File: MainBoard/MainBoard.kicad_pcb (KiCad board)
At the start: 6 copper layers, 45 x 45 mm, 110 parts, among them J1 0015912060 Molex, J2 USB4110-GF-A, J3 M55-7104042R, Q1 PMV19XNEAR, Q2 PMV19XNEAR, Q3 PMV19XNEAR, Q4 PMV19XNEAR, SW1 SW_TL1015AF160QG, SW2 SW_TL1015AF160QG, U1 INA185A4IDRLR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

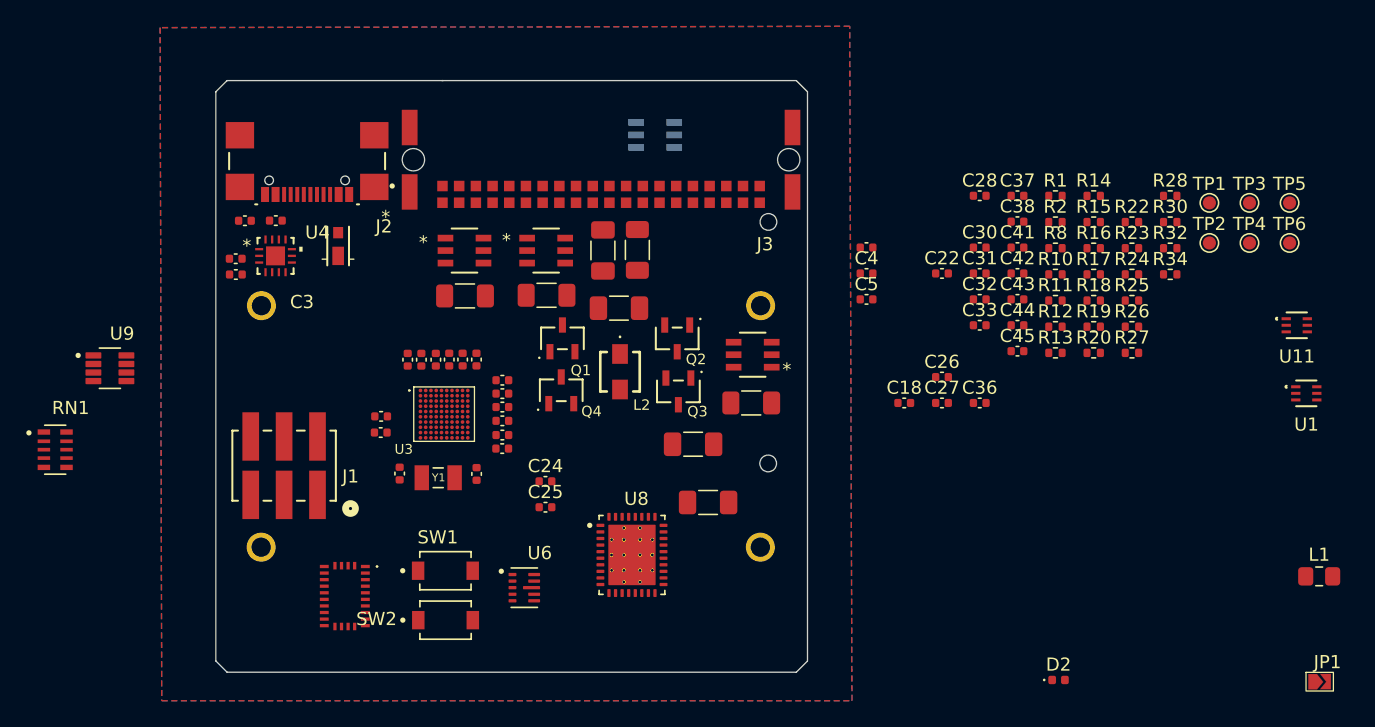
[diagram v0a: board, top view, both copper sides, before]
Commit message: Waiting on board sizes to finish placement
All parts placed, some light schematic and checking work still needs to be done
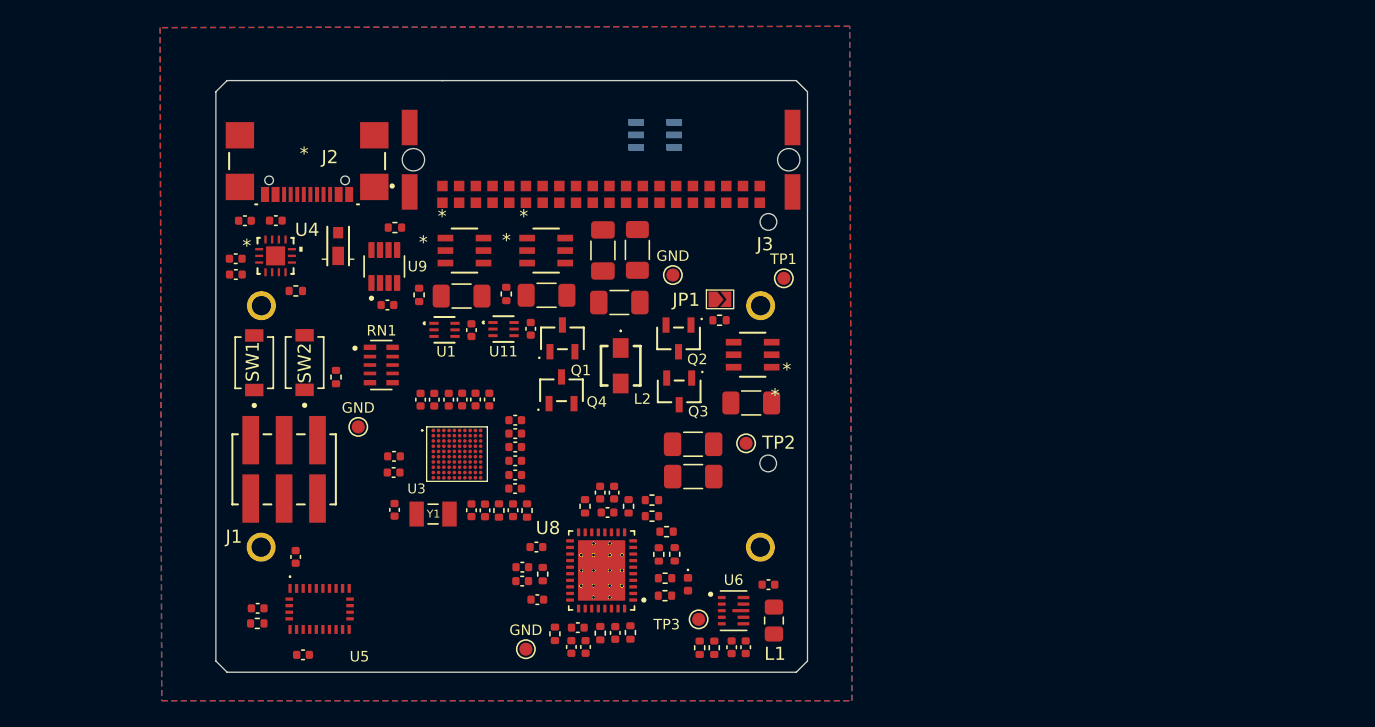
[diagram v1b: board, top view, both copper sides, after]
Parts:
- removed TP4: GND, TestPoint:TestPoint_Pad_D1.0mm
- added GND: GND, TestPoint:TestPoint_Pad_D1.0mm, F.Cu at (104.2, 56.5)
- moved GND 72.9 mm to (80.2, 68.1)
- moved R10 66.3 mm to (72.5, 83.0)
- moved GND 65.8 mm to (93.0, 85.0)
- moved U1 65.7 mm to (86.8, 60.7)
- moved R22 61.7 mm to (78.5, 64.3), turned to -90 degrees
- moved U11 60.3 mm to (91.3, 60.7)
- moved R8 57.9 mm to (75.5, 57.8)
- moved R32 57.2 mm to (84.9, 58.1), turned to 90 degrees
- moved R25 56.3 mm to (83.0, 52.9), turned to 180 degrees
- moved JP1 54.1 mm to (107.7, 58.4)
- moved C22 53.7 mm to (75.5, 78.0), turned to 90 degrees
- moved R23 52.8 mm to (95.2, 83.8), turned to -90 degrees
- moved TP3 52.5 mm to (106.1, 82.7)
- moved C5 51.9 mm to (72.6, 81.9)
- moved C4 51.8 mm to (76.0, 85.4), turned to 180 degrees
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- renumbered TP6 to GND, TP5 to GND

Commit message: Still waiting on final board size....
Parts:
- added R35: 100k, Resistor_SMD:R_0402_1005Metric, B.Cu at (108.5, 46.0)
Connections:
- U2 pad 3: unconnected-(U2-G-Pad3) -> HEATER_ENABLE
- U2 pad 4: unconnected-(U2-S-Pad4) -> BAT+
- U3 pad E1: unconnected-(U3A-PC8-PadE1) -> HEATER_ENABLE
- U3 pad E4: unconnected-(U3A-PC7-PadE4) -> EXTERNAL_BAT_CUTOFF
- U3 pad F3: unconnected-(U3A-PD14-PadF3) -> BAT_PULLDOWN
- U3 pad G4: unconnected-(U3A-PE14-PadG4) -> IMU_NRST
- U3 pad H4: unconnected-(U3A-PE15-PadH4) -> IMU_PSO/WAKE_GPIO
- U3 pad J5: unconnected-(U3A-PE9-PadJ5) -> BATMANG_INT_DIN
- U3 pad K4: unconnected-(U3A-PE11-PadK4) -> EXTERNAL_3.3V_CUTOFF
- U3 pad K5: unconnected-(U3A-PE8-PadK5) -> IMU_PSO/WAKE_GPIO
- U3 pad K6: unconnected-(U3A-PE7-PadK6) -> USBC_PD_INT_N
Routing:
- net +3.3V: track 0.00 -> 42.3 mm, vias 0 -> 7
- net USB_D-: track 0.00 -> 2.08 mm, vias 0 -> 1
- net USB_D+: track 0.00 -> 2.08 mm, vias 0 -> 1
- net GND: track 0.00 -> 1.18 mm, vias 0 -> 6
- net USBC_PD_INT_N: vias 0 -> 1
- net SWO: vias 0 -> 1
- net PARENT_SPI3_SCK: vias 0 -> 1
- net PARENT_SPI3_NSS: vias 0 -> 1
- net PARENT_SPI3_MOSI: vias 0 -> 1
- net PARENT_SPI3_MISO: vias 0 -> 1
- net Net-(U3A-PC15-OSC32_OUT): vias 0 -> 1
- net Net-(U3A-PC14-OSC32_IN): vias 0 -> 1
- net Net-(U3A-PA2): vias 0 -> 1
- net Net-(U3A-PA1): vias 0 -> 1
- net NRST: vias 0 -> 1
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
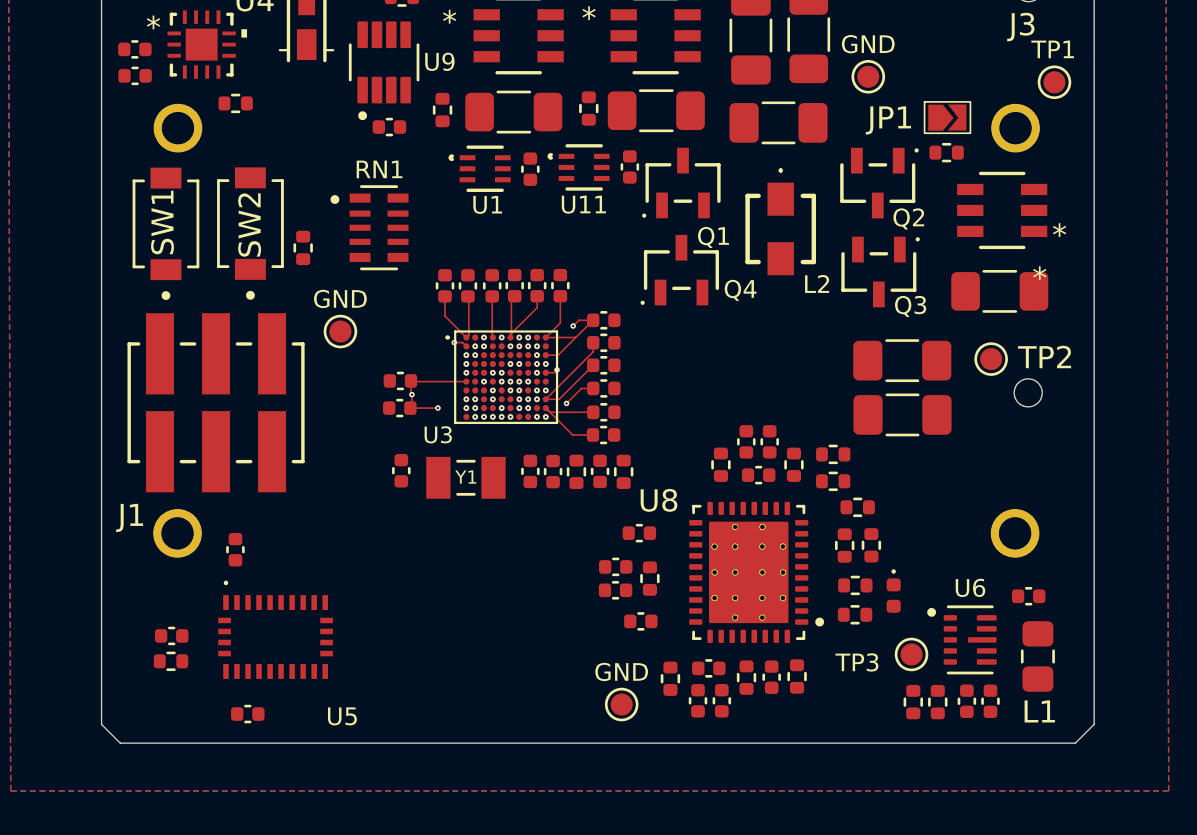
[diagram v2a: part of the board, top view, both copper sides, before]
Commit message: Cap routing
Capacitor Routing near STM, can be moved around if needed
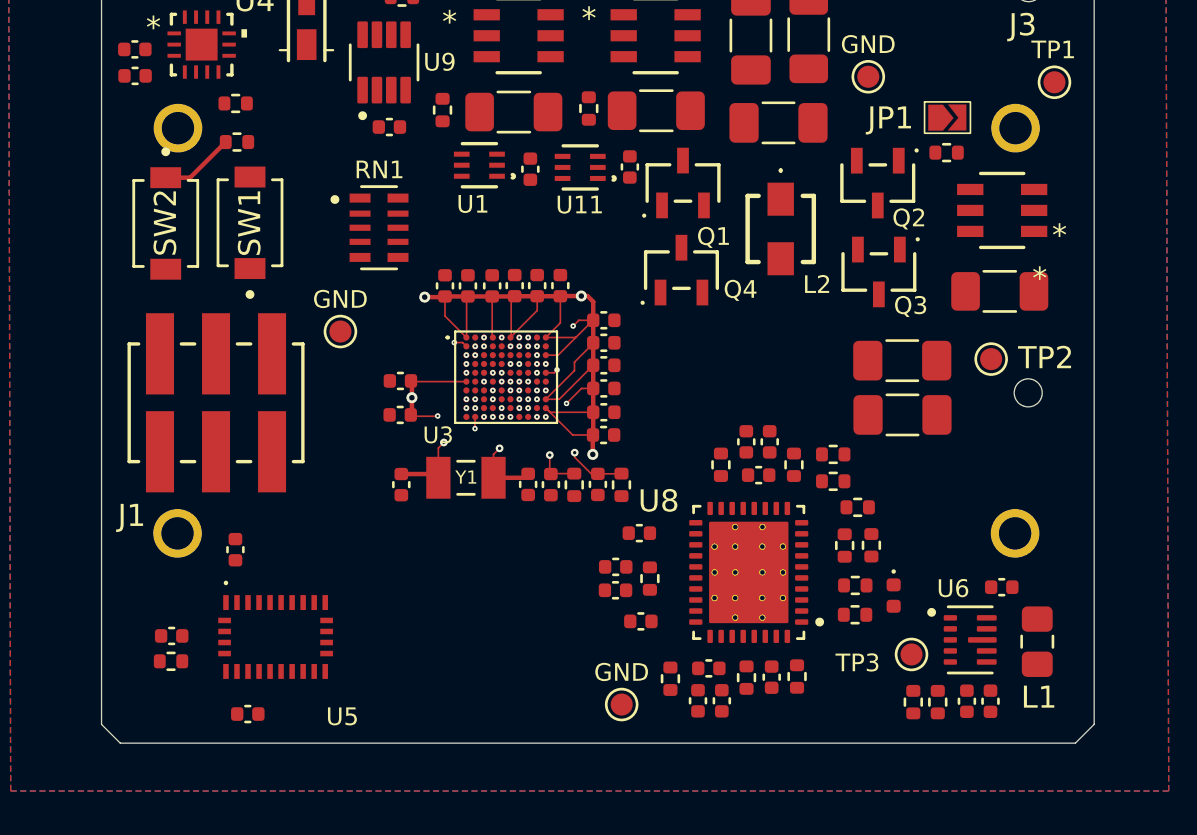
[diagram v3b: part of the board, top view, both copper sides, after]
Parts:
- moved R22 5.66 mm to (75.5, 59.5), turned to 180 degrees
- moved SW2 3.84 mm to (72.3, 63.2), turned to -90 degrees
- moved SW1 3.81 mm to (76.1, 63.2)
- moved C18 1.29 mm to (110.2, 79.7)
- moved L1 0.67 mm to (111.8, 82.2)
- moved C29 0.63 mm to (83.0, 75.0)
- moved C24 0.60 mm to (89.8, 75.0)
- moved C46 0.60 mm to (88.7, 75.0)
- moved R1 0.60 mm to (90.8, 75.0)
- moved C25 0.60 mm to (91.9, 75.0)
- moved R2 0.60 mm to (93.0, 75.0)
- moved C17 0.31 mm to (82.9, 71.9)
- moved U1 0.31 mm to (86.5, 60.6), turned to 180 degrees
- moved U11 0.18 mm to (91.1, 60.7), turned to 180 degrees
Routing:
- net +3.3V: track 42.3 -> 57.1 mm, vias 7 -> 10
- net Net-(U3A-PC15-OSC32_OUT): track 0.00 -> 10.8 mm, vias 1 -> 2
- net Net-(U3A-PC14-OSC32_IN): track 0.00 -> 8.81 mm, vias 1 -> 2
- net Net-(U3A-PA2): track 0.00 -> 6.14 mm, vias 1 -> 2
- net Net-(U3A-PA1): track 0.00 -> 5.66 mm, vias 1 -> 2
- net BOOT0: track 0.00 -> 3.39 mm
- net GND: track 1.18 -> 1.72 mm

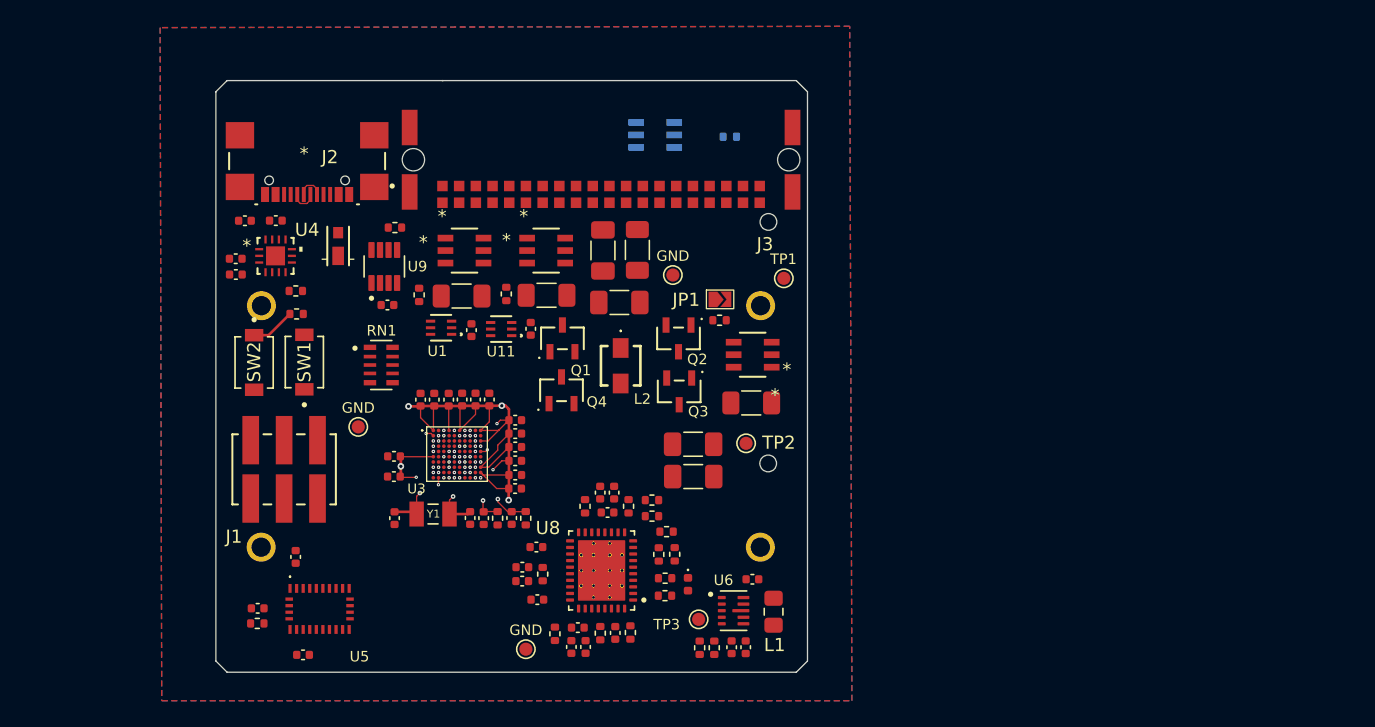
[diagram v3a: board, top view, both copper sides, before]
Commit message: Happy with placement
Got sizes from mechanical, adjusted placement accordingly
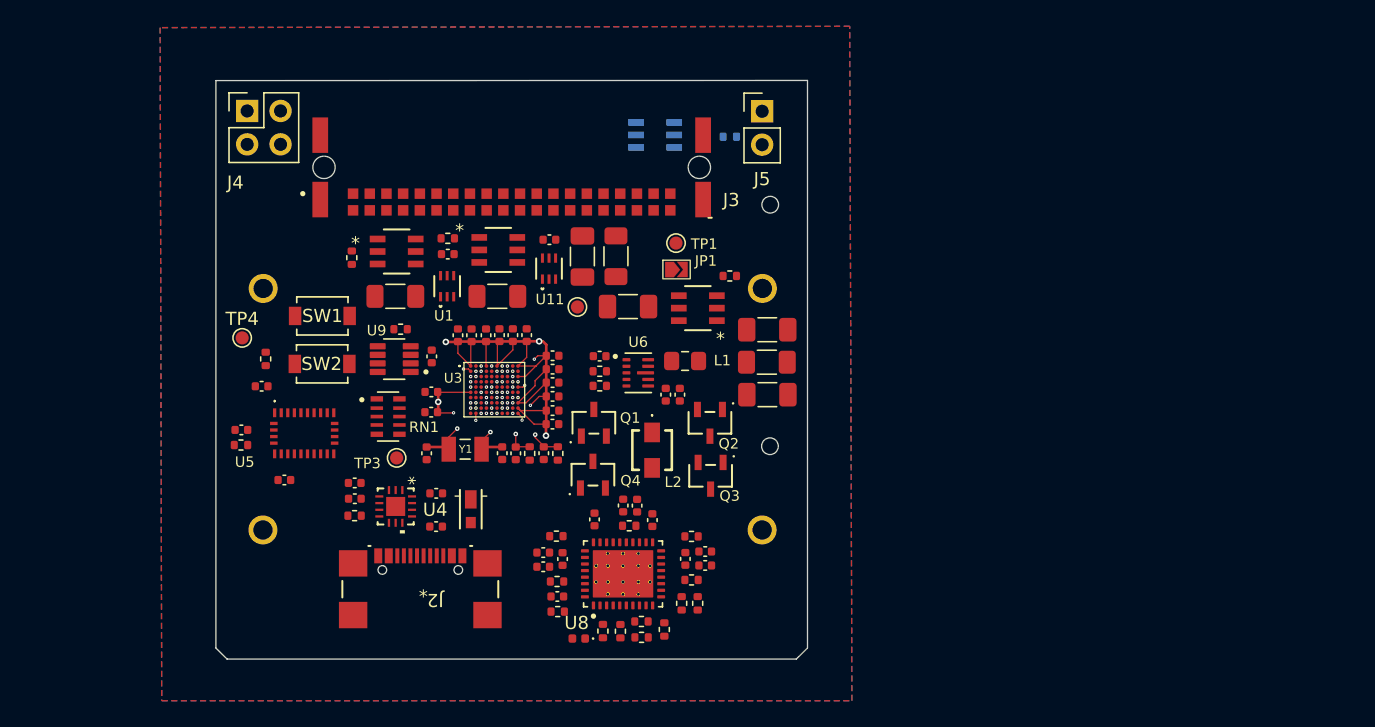
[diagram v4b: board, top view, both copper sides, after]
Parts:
- removed GND (x3): GND, TestPoint:TestPoint_Pad_D1.0mm
- removed J1: 0015912060 Molex, inspirefly:CONN_713080000-SD_06_M6p10_MOL
- added J4: Conn_01x04_Pin, Connector_PinHeader_2.54mm:PinHeader_2x02_P2.54mm_Vertical, F.Cu at (71.8, 44.1)
- added J5: Conn_01x02_Pin, Connector_PinHeader_2.54mm:PinHeader_1x02_P2.54mm_Vertical, F.Cu at (111.0, 44.1)
- added TP4: GND, TestPoint:TestPoint_Pad_D1.0mm, F.Cu at (71.4, 61.3)
- moved J2 35.3 mm to (85.0, 81.3), turned to 0 degrees
- moved C7 26.3 mm to (86.2, 75.7)
- moved TP3 26.0 mm to (83.2, 70.5)
- moved C6 25.3 mm to (86.2, 73.2), turned to 0 degrees
- moved D1 22.4 mm to (88.8, 74.4), turned to -90 degrees
- moved R12 22.4 mm to (98.6, 63.9), turned to 180 degrees
- moved R11 21.7 mm to (98.6, 65.0), turned to 180 degrees
- moved U4 21.1 mm to (83.1, 74.2), turned to -90 degrees
- moved C18 20.6 mm to (98.6, 62.7), turned to 180 degrees
- moved L1 20.2 mm to (105.1, 63.1), turned to 0 degrees
- moved C26 19.9 mm to (104.7, 65.7)
- moved C27 19.9 mm to (103.6, 65.7)
- moved BT2 19.7 mm to (92.0, 57.6)
- moved U6 19.5 mm to (101.5, 64.0)
- moved C1 19.3 mm to (80.0, 72.4)
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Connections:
- J3 pad B11: EXTERNAL_VOLTAGE -> GND
- J3 pad B12: EXTERNAL_VOLTAGE -> unconnected-(J3-PadB12)
- J3 pad B13: EXTERNAL_VOLTAGE -> unconnected-(J3-PadB13)
- J3 pad B14: EXTERNAL_VOLTAGE -> unconnected-(J3-PadB14)
- J3 pad B15: unconnected-(J3-PadB15) -> EXTERNAL_VOLTAGE
- J3 pad B16: unconnected-(J3-PadB16) -> EXTERNAL_VOLTAGE
- J3 pad B17: unconnected-(J3-PadB17) -> EXTERNAL_VOLTAGE
- J3 pad B18: GND -> EXTERNAL_VOLTAGE
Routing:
- net BOOT0: track 3.39 -> 0.00 mm
- net USB_D-: track 2.08 -> 0.00 mm
- net USB_D+: track 2.08 -> 0.00 mm
- net GND: track 1.72 -> 2.38 mm
- net Net-(U3A-PC15-OSC32_OUT): track 10.8 -> 11.4 mm
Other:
- board size 45 x 45 mm -> 45 x 44 mm

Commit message: Added some routing
Routing done for f.cu BQ chip and some others
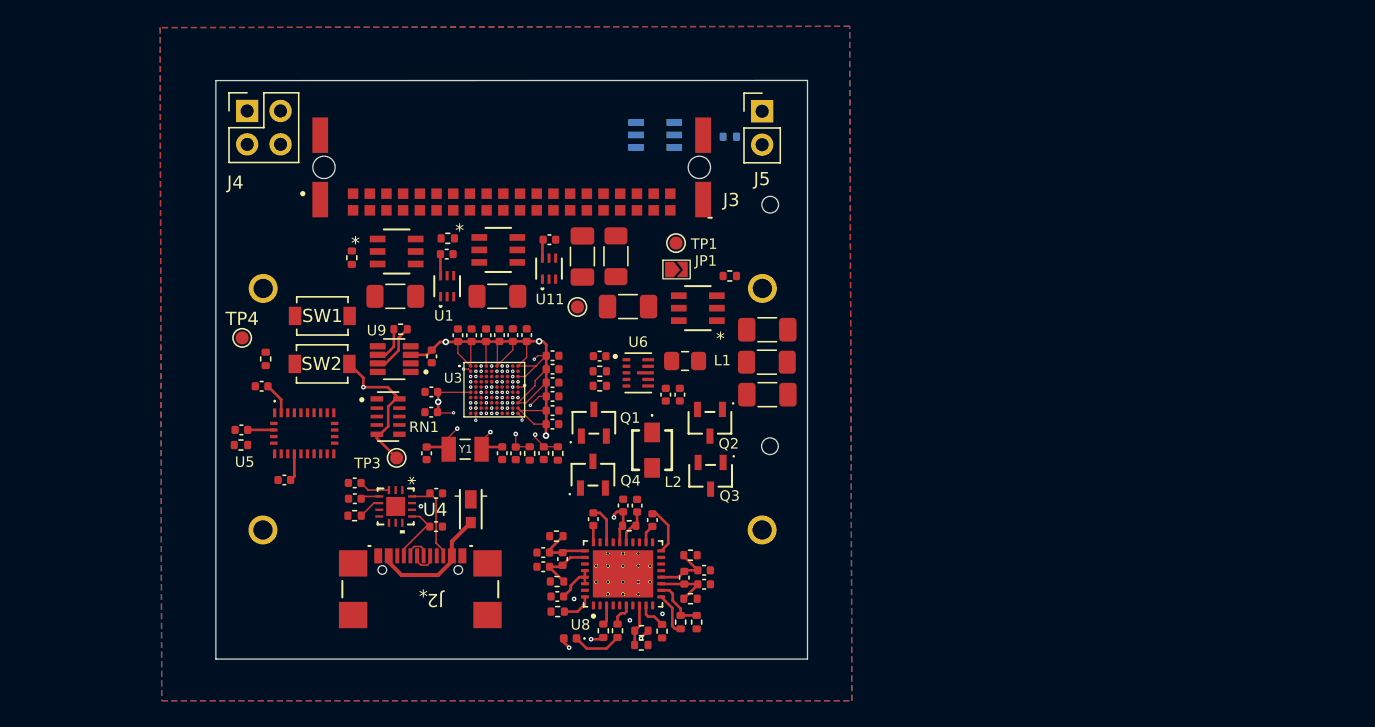
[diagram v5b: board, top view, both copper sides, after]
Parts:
- moved C43 1.43 mm to (106.5, 79.0)
- moved R14 1.43 mm to (104.8, 83.0)
- moved R15 1.43 mm to (106.0, 83.0)
- moved R30 1.43 mm to (105.5, 81.2)
- moved C44 1.43 mm to (105.0, 79.6)
- moved C45 1.43 mm to (106.5, 80.1)
- moved R28 1.43 mm to (105.5, 77.9)
- moved R16 0.70 mm to (101.8, 83.6)
- moved D2 0.65 mm to (96.3, 84.2)
- moved R17 0.58 mm to (101.8, 84.7), turned to 0 degrees
- moved R26 0.22 mm to (100.0, 83.6)
- moved R19 0.21 mm to (103.3, 83.6)
- moved C41 0.09 mm to (98.1, 75.1)
- moved C3 0.08 mm to (87.0, 55.0)
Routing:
- net +3.3V: track 57.1 -> 83.9 mm, vias 10 -> 12
- net REGN: track 0.00 -> 21.2 mm, vias 0 -> 3
- net Net-(D1-A): track 0.00 -> 9.66 mm
- net Net-(J2-CC2): track 0.00 -> 6.63 mm
- net Net-(J2-CC1): track 0.00 -> 4.87 mm
- net SRP: track 0.00 -> 4.60 mm
- net ACP: track 0.00 -> 4.55 mm
- net ACN: track 0.00 -> 4.43 mm
- net SRN: track 0.00 -> 4.35 mm
- net Net-(U8-FB): track 0.00 -> 4.11 mm
- net CAN_H: track 0.00 -> 3.89 mm
- net Net-(D2-K): track 0.00 -> 3.78 mm
- net BAT_SIDE_INDUC: track 0.00 -> 3.74 mm
- net EXTERNAL_VOLTAGE: track 0.00 -> 3.39 mm
- net Net-(U8-FBG): track 0.00 -> 3.29 mm
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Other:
- outline, holes or cut-outs redrawn
